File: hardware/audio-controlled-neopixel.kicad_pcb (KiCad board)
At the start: 2 copper layers, 98 x 62 mm, 63 parts, among them J1 Phoenix MPT, J2 Conn_01x01_Female, J3 Phoenix MPT 3, J4 Phoenix MKDS 2, J5 Conn_01x01_Female, J6 Conn_01x01_Female, J7 Conn_01x01_Female, SW1 SW_SPST, U1 NE5532, U2 NE5532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

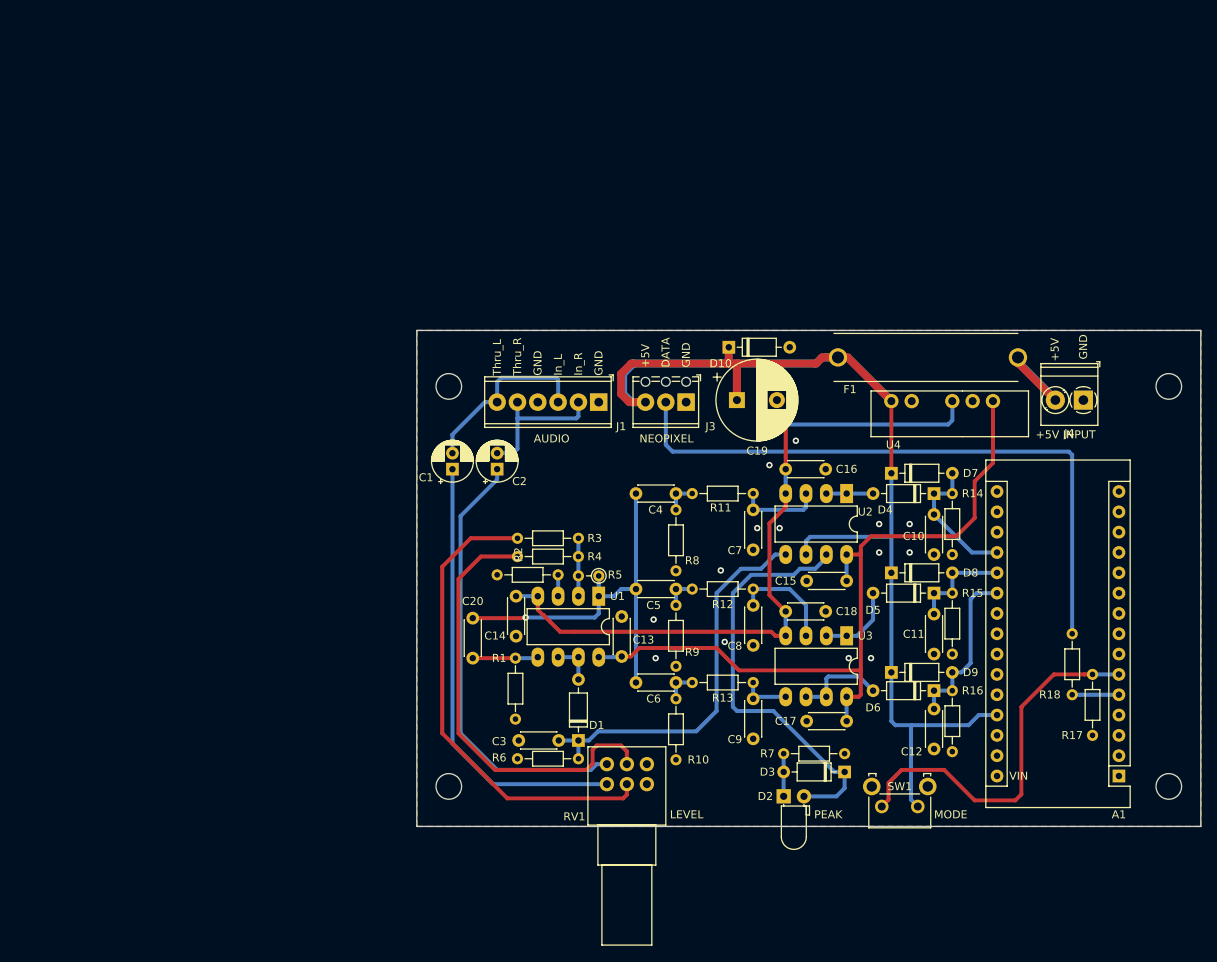
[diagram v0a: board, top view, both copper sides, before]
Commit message: Updated schematic and PCB to use SMD components for ease of manufacture.
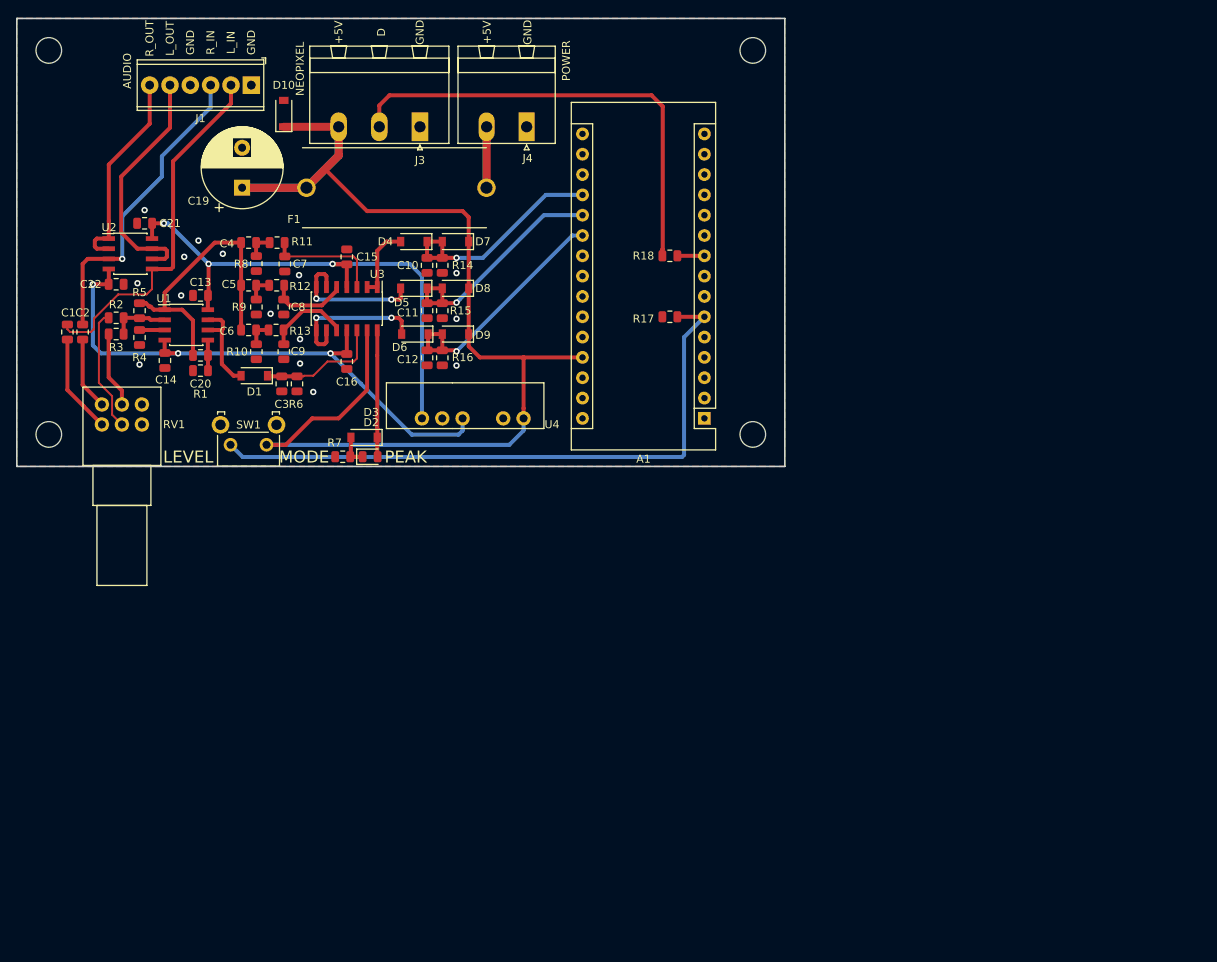
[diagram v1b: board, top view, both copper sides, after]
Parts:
- removed C17, C18: 100n, Capacitor_THT:C_Disc_D4.3mm_W1.9mm_P5.00mm
- added C21: 100n, Capacitor_SMD:C_0805_2012Metric, F.Cu at (54.0, 54.6)
- added C22: 100n, Capacitor_SMD:C_0805_2012Metric, F.Cu at (50.4, 62.2)
- C1, C2: footprint Capacitor_THT:CP_Radial_D5.0mm_P2.00mm -> Capacitor_SMD:C_0805_2012Metric
- C10, C11, C12, C13, C14, C15, C16, C20, C3, C4, C5, C6, C7, C8, C9: footprint Capacitor_THT:C_Disc_D4.3mm_W1.9mm_P5.00mm -> Capacitor_SMD:C_0805_2012Metric
- D1, D4, D5, D6: footprint Diode_THT:D_DO-35_SOD27_P7.62mm_Horizontal -> Diode_SMD:D_SOD-123
- D10, D3, D7, D8, D9: value BAT85 -> 1N5819; footprint Diode_THT:D_DO-35_SOD27_P7.62mm_Horizontal -> Diode_SMD:D_SOD-123
- D2: footprint LED_THT:LED_D3.0mm_Horizontal_O1.27mm_Z2.0mm -> LED_SMD:LED_0805_2012Metric
- F1: value 611-9302 -> 176-9047
- J3: value Phoenix MPT 3 -> KF2EDGK; footprint TerminalBlock_Phoenix:TerminalBlock_Phoenix_MPT-0,5-3-2.54_1x03_P2.54mm_Horizontal -> Connector_Phoenix_MSTB:PhoenixContact_MSTBA_2,5_3-G-5,08_1x03_P5.08mm_Horizontal
- J4: value Phoenix MKDS 2 -> KF2EDGK; footprint TerminalBlock_Phoenix:TerminalBlock_Phoenix_PT-1,5-2-3.5-H_1x02_P3.50mm_Horizontal -> Connector_Phoenix_MSTB:PhoenixContact_MSTBA_2,5_2-G_1x02_P5.00mm_Horizontal
- R1, R11, R13, R14, R15, R16, R17, R18, R2, R3, R4, R6, R7, R8, R9: footprint Resistor_THT:R_Axial_DIN0204_L3.6mm_D1.6mm_P7.62mm_Horizontal -> Resistor_SMD:R_0805_2012Metric
- R10, R12: value 4K7 -> 7K5; footprint Resistor_THT:R_Axial_DIN0204_L3.6mm_D1.6mm_P7.62mm_Horizontal -> Resistor_SMD:R_0805_2012Metric
- R5: value 100K -> 200K; footprint Resistor_THT:R_Axial_DIN0204_L3.6mm_D1.6mm_P2.54mm_Vertical -> Resistor_SMD:R_0805_2012Metric
- U1: value NE5532 -> LM358; footprint Package_DIP:DIP-8_W7.62mm_LongPads -> Package_SO:SOIC-8_3.9x4.9mm_P1.27mm
- U2: footprint Package_DIP:DIP-8_W7.62mm_LongPads -> Package_SO:SOIC-8_3.9x4.9mm_P1.27mm
- U3: value NE5532 -> LM324; footprint Package_DIP:DIP-8_W7.62mm_LongPads -> Package_SO:SOIC-14_3.9x8.7mm_P1.27mm
- moved J6 146.8 mm to (42.0, 81.0)
- moved J2 99.5 mm to (130.0, 33.0)
- moved U2 94.4 mm to (52.2, 58.4), turned to 0 degrees
- moved SW1 93.1 mm to (69.2, 82.3)
- moved D6 78.7 mm to (87.8, 68.5)
- moved J4 77.5 mm to (101.7, 42.5)
- moved RV1 77.5 mm to (48.6, 79.8)
- moved C12 77.1 mm to (89.3, 71.4)
- moved R16 76.1 mm to (91.2, 71.4)
- moved D5 75.4 mm to (87.6, 62.7)
- moved U3 74.7 mm to (79.2, 65.3)
- moved R18 74.4 mm to (119.6, 58.7), turned to 180 degrees
- moved R17 74.4 mm to (119.6, 66.3), turned to 0 degrees
- moved R13 74.2 mm to (70.4, 67.9)
- moved C11 73.9 mm to (89.3, 65.5)
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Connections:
- J1 pad 2: /Input_R -> /Input_L
- J1 pad 3: /Input_L -> /Input_R
- J1 pad 5: /Input_R -> /Passthru_L
- J1 pad 6: /Input_L -> /Passthru_R
- R18 pad 1: Net-(A1-Pad5) -> Net-(A1-Pad9)
- U2 pad 1: Net-(D4-Pad2) -> /Passthru_R
- U2 pad 2: Net-(D4-Pad2) -> /Passthru_R
- U2 pad 3: Net-(C7-Pad2) -> /Input_R
- U2 pad 5: Net-(C3-Pad1) -> /Input_L
- U2 pad 6: +5V -> /Passthru_L
- U2 pad 7: Net-(D2-Pad2) -> /Passthru_L
- U3 pad 1: Net-(D5-Pad2) -> Net-(D4-Pad2)
- U3 pad 2: Net-(D5-Pad2) -> Net-(D4-Pad2)
- U3 pad 3: Net-(C8-Pad1) -> Net-(C7-Pad2)
- U3 pad 4: -12V -> +12V
- U3 pad 5: Net-(C9-Pad1) -> Net-(C8-Pad1)
- U3 pad 6: Net-(D6-Pad2) -> Net-(D5-Pad2)
- U3 pad 7: Net-(D6-Pad2) -> Net-(D5-Pad2)
- U3 pad 8: +12V -> Net-(D6-Pad2)
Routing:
- net Net-(C2-Pad1): track 55.4 -> 9.08 mm
- net Net-(R3-Pad2): track 55.0 -> 9.49 mm
- net Net-(R2-Pad1): track 59.6 -> 15.4 mm
- net Net-(C1-Pad1): track 55.7 -> 12.4 mm
- net Net-(D2-Pad2): track 53.0 -> 15.8 mm
- net Net-(C3-Pad1): track 48.9 -> 15.7 mm
- net Net-(A1-Pad6): track 47.3 -> 79.1 mm
- net /Passthru_L: track 0.00 -> 30.3 mm
- net +12V: track 94.7 -> 66.6 mm, vias 0 -> 3
- net /Passthru_R: track 0.00 -> 25.8 mm
- net /Input_L: track 22.9 -> 45.3 mm
- net /Neopixel: track 79.0 -> 57.9 mm
- net /Input_R: track 18.1 -> 39.1 mm, vias 0 -> 1
- net +5V: track 175.6 -> 158.1 mm
- net /Mid_out: track 13.0 -> 29.6 mm, vias 0 -> 1
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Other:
- board size 98 x 62 mm -> 96 x 56 mm
- board text added: "D"
- board text added: "L_IN"
- board text added: "L_OUT"
- board text added: "POWER"
- board text added: "R_IN"
- board text added: "R_OUT"
- board text removed: "+5V INPUT"
- board text removed: "DATA"
- board text removed: "In_L"
- board text removed: "In_R"
- board text removed: "Thru_L"
- board text removed: "Thru_R"
- board text removed: "VIN"

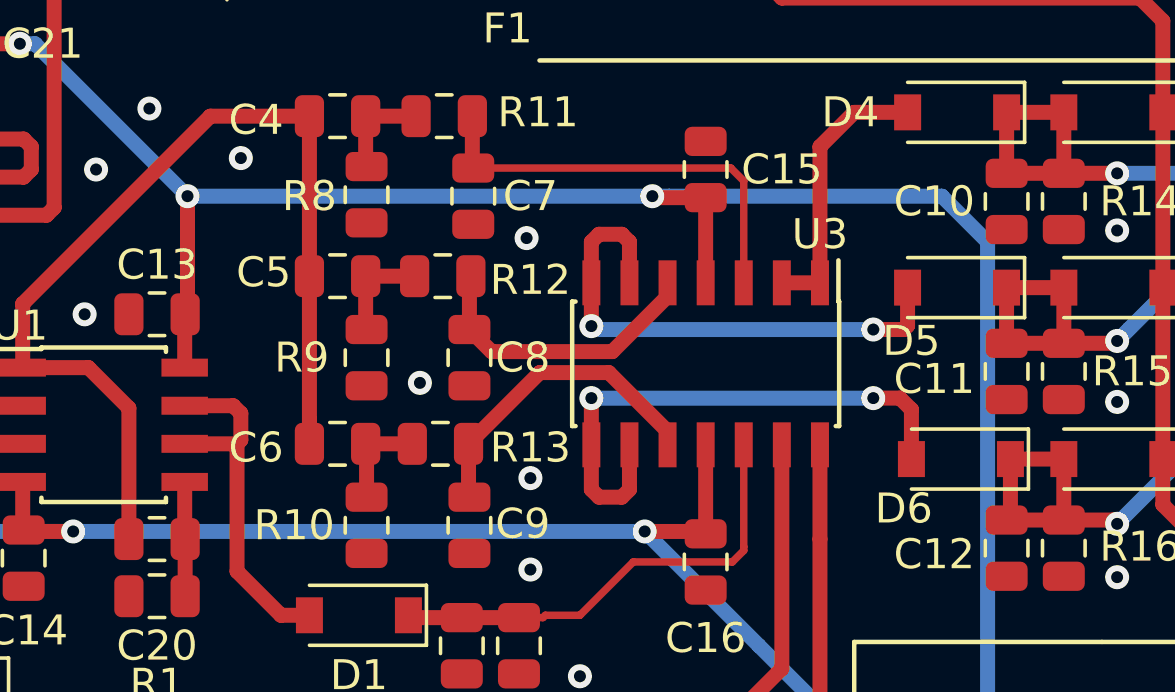
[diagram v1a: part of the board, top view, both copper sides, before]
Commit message: Fixed minor PCB trace issues
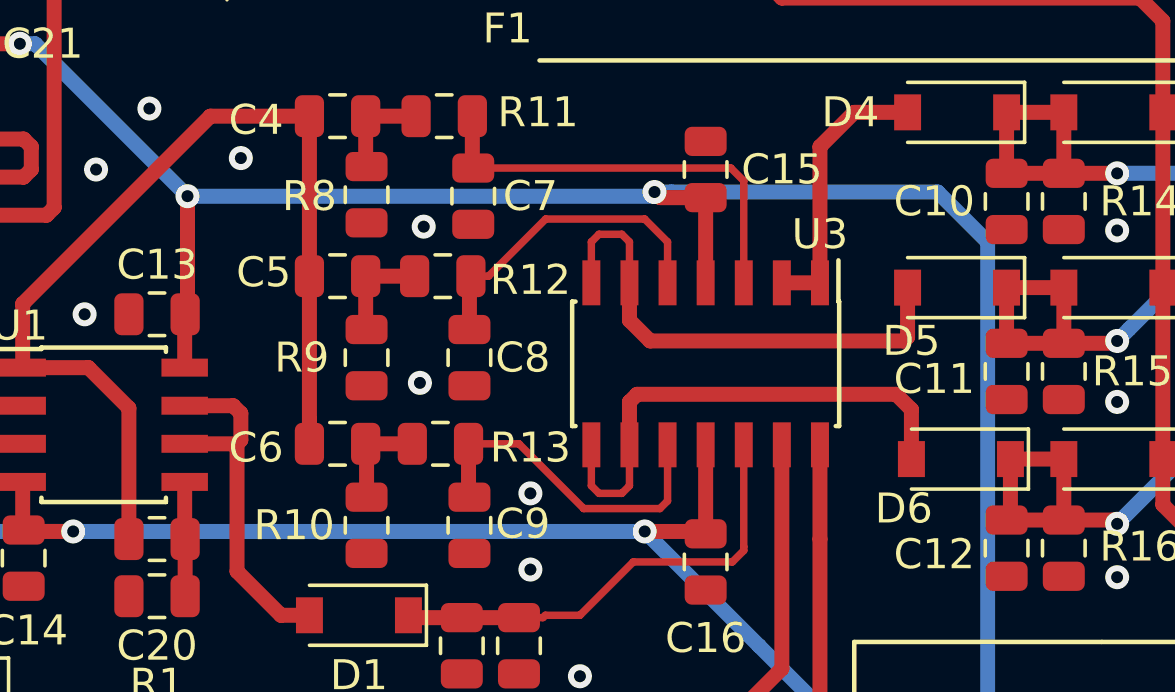
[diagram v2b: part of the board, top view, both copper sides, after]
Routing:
- net Net-(D6-Pad2): track 18.5 -> 17.0 mm, vias 2 -> 0
- net Net-(C8-Pad1): track 9.92 -> 10.8 mm
- net Net-(D5-Pad2): track 17.6 -> 16.7 mm, vias 2 -> 0
- net Net-(C9-Pad1): track 10.7 -> 11.3 mm

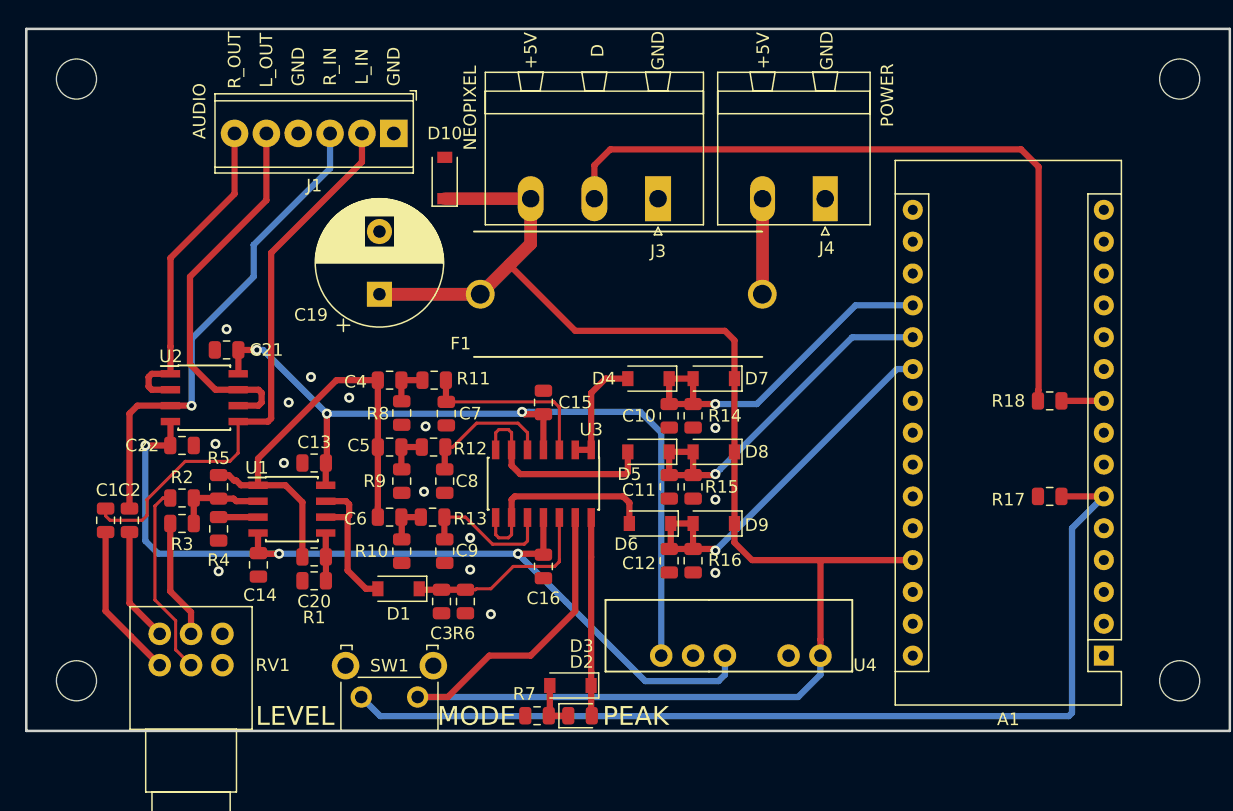
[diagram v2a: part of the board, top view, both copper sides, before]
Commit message: updated schematic to reduce component count, PCB update to match
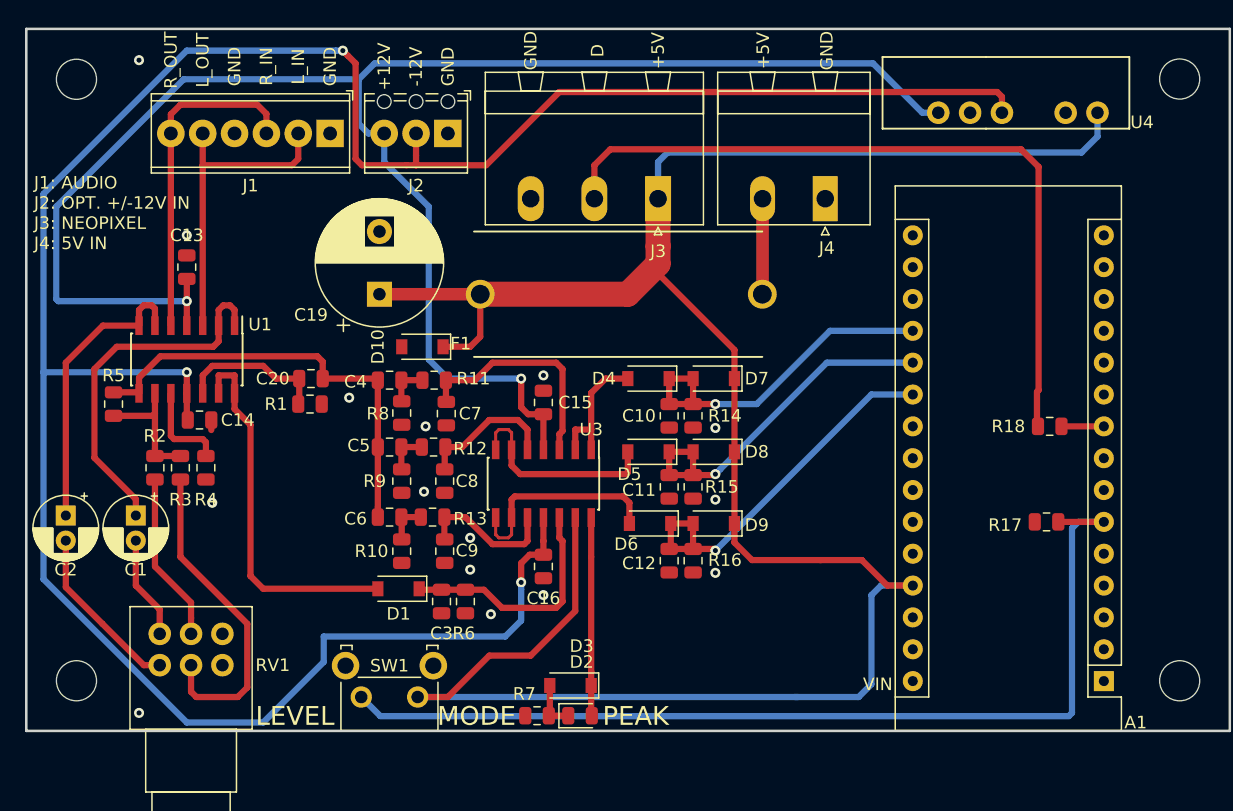
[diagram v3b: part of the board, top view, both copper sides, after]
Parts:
- removed C21, C22: 100n, Capacitor_SMD:C_0805_2012Metric
- removed U2: NE5532, Package_SO:SOIC-8_3.9x4.9mm_P1.27mm
- added J8: Conn_01x01_Female, MountingHole:MountingHole_3.2mm_M3, F.Cu at (42.0, 33.0)
- C1, C2: footprint Capacitor_SMD:C_0805_2012Metric -> Capacitor_THT:CP_Radial_D5.0mm_P2.00mm
- C10, C11, C12, C3: value 1u -> 100n
- C19: value EEUFM1C102 -> 330u 35V
- J2: value Conn_01x01_Female -> KF2EDGK; footprint MountingHole:MountingHole_3.2mm_M3 -> TerminalBlock_Phoenix:TerminalBlock_Phoenix_MPT-0,5-3-2.54_1x03_P2.54mm_Horizontal
- R14, R15, R16: value 100K -> 1M
- RV1: value 10K -> 10KA
- U1: value LM358 -> LM324; footprint Package_SO:SOIC-8_3.9x4.9mm_P1.27mm -> Package_SO:SOIC-14_3.9x8.7mm_P1.27mm
- moved J5 100.2 mm to (130.0, 81.0)
- moved J2 58.5 mm to (71.6, 37.3), turned to 180 degrees
- moved U4 48.6 mm to (126.0, 31.2)
- moved J7 48.0 mm to (130.0, 33.0)
- moved C13 18.6 mm to (50.8, 48.0), turned to 270 degrees
- moved U1 14.6 mm to (50.8, 55.4), turned to 270 degrees
- moved C20 14.2 mm to (60.7, 56.9), turned to 0 degrees
- moved R1 14.1 mm to (60.6, 58.9), turned to 0 degrees
- moved D10 13.6 mm to (69.6, 54.4), turned to 180 degrees
- moved C14 12.5 mm to (51.8, 60.2), turned to 0 degrees
- moved R5 10.7 mm to (45.0, 58.9)
- moved C2 5.09 mm to (41.1, 67.8), turned to 270 degrees
- moved J1 5.08 mm to (62.2, 37.3)
- moved R4 4.98 mm to (52.3, 64.0)
- moved R3 4.45 mm to (50.3, 64.0), turned to 270 degrees
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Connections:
- net /High_out renamed /High
- net /Low_out renamed /Low
- net /Mid_out renamed /Mid
- C1 pad 2: /Input_L -> Net-(C1-Pad2)
- C2 pad 2: /Input_R -> Net-(C2-Pad2)
- J1 pad 5: /Passthru_L -> /Input_L
- J1 pad 6: /Passthru_R -> /Input_R
- J2 pad 1: Net-(J2-Pad1) -> GND
- J3 pad 1: GND -> +5V
- J3 pad 3: +5V -> GND
- RV1 pad 1: Net-(C1-Pad1) -> Net-(C2-Pad2)
- RV1 pad 2: Net-(R2-Pad1) -> Net-(R3-Pad2)
- RV1 pad 4: Net-(C2-Pad1) -> Net-(C1-Pad2)
- RV1 pad 5: Net-(R3-Pad2) -> Net-(R2-Pad1)
- U1 pad 1: /Buf_input -> Net-(C1-Pad1)
- U1 pad 2: Net-(R2-Pad2) -> Net-(C1-Pad1)
- U1 pad 3: Net-(R4-Pad1) -> /Input_L
- U1 pad 4: -12V -> +12V
- U1 pad 5: Net-(C20-Pad1) -> /Input_R
- U1 pad 6: Net-(D1-Pad2) -> Net-(C2-Pad1)
- U1 pad 7: Net-(D1-Pad2) -> Net-(C2-Pad1)
- U1 pad 8: +12V -> /Buf_input
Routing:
- net -12V: track 72.4 -> 198.8 mm
- net +12V: track 66.7 -> 138.8 mm, vias 3 -> 2
- net /Passthru_L: track 30.3 -> 0.00 mm
- net +5V: track 158.1 -> 187.0 mm
- net /Passthru_R: track 25.8 -> 0.00 mm
- net /Input_L: track 45.3 -> 25.2 mm
- net Net-(D1-Pad2): track 12.1 -> 29.8 mm
- net Net-(C1-Pad1): track 12.4 -> 29.2 mm
- net Net-(R3-Pad2): track 9.49 -> 25.9 mm
- net Net-(C2-Pad1): track 9.08 -> 23.4 mm
- net Net-(C2-Pad2): track 0.00 -> 13.8 mm
- net /Input_R: track 39.1 -> 26.7 mm, vias 1 -> 0
- net Net-(C1-Pad2): track 0.00 -> 8.23 mm
- net Net-(C20-Pad1): track 3.82 -> 11.9 mm
- net Net-(R4-Pad1): track 3.14 -> 7.49 mm
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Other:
- board text added: "+12V"
- board text added: "-12V"
- board text added: "J1: AUDIO J2: OPT. +/-12V IN J3: NEOPIXEL J4: 5V IN"
- board text added: "VIN"
- board text removed: "AUDIO"
- board text removed: "NEOPIXEL"
- board text removed: "POWER"

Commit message: minor PCB clean up
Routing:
- net Net-(D6-Pad2): track 17.0 -> 15.7 mm
- net Net-(D5-Pad2): track 16.7 -> 15.8 mm
